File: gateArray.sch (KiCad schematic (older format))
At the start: 56 parts, among them IC101 AMS40489, IC108 MC74HC4051N, IC109 LA6393D, X181 40MhZ

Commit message: more accurate on pins definition, power, centronic 36, jack, and some wiring
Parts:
- removed C128: 39P, symbol Device:C_Small
- removed C129: 47P, symbol Device:C_Small
- removed L102: L, symbol Device:L
- removed R145: 4,7M, symbol Device:R_Small_US
- removed X181: 40MhZ, Oscillator:Oscillator_DIP-8, symbol Device:Crystal
- added X181: 40 MHz, Oscillator:Oscillator_DIP-14, symbol Oscillator:ACO-xxxMHz
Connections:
- wire segments 409 -> 387
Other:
- note removed: "40MhZ\nOSC"
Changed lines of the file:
@@
 Wire Wire Line
 	6950 5550 6850 5550
-Wire Wire Line
-	7250 5400 7250 6500
 $Comp
 L power:+5V #PWR0113
@@
 Connection ~ 2850 4050
 Wire Wire Line
-	2850 4050 2500 4050
-Wire Wire Line
 	3200 3200 3200 3100
 Wire Wire Line
@@
 Wire Wire Line
 	2050 3950 2050 4050
-Wire Wire Line
-	2350 4050 2050 4050
 Connection ~ 2050 4050
 Wire Wire Line
@@
 	1    0    0    -1
 $EndComp
-$Comp
-L Device:C_Small C128
-U 1 1 6120AEE9
-P 6450 7050
-F 0 "C128" H 6542 7096 50  0000 L CNN
-F 1 "39P" H 6542 7005 50  0000 L CNN
-F 2 "" H 6450 7050 50  0001 C CNN
-F 3 "~" H 6450 7050 50  0001 C CNN
-	1    6450 7050
-	1    0    0    -1
-$EndComp
 Wire Wire Line
 	5100 7400 5150 7400
@@
 Wire Wire Line
 	4550 7400 4600 7400
-Wire Wire Line
-	6450 7150 6450 7250
 $Comp
 L power:GND #PWR0106
 U 1 1 61400741
-P 6800 7350
-F 0 "#PWR0106" H 6800 7100 50  0001 C CNN
-F 1 "GND" H 6805 7177 50  0000 C CNN
-F 2 "" H 6800 7350 50  0001 C CNN
-F 3 "" H 6800 7350 50  0001 C CNN
-	1    6800 7350
+P 6850 6600
+F 0 "#PWR0106" H 6850 6350 50  0001 C CNN
+F 1 "GND" H 6855 6427 50  0000 C CNN
+F 2 "" H 6850 6600 50  0001 C CNN
+F 3 "" H 6850 6600 50  0001 C CNN
+	1    6850 6600
 	1    0    0    -1
 $EndComp
@@
 	6350 5400 6350 6800
 Wire Wire Line
-	7150 5400 7150 6350
+	7150 5400 7150 6300
 Wire Wire Line
 	6050 6950 6050 6800
@@
 Wire Wire Line
 	4550 6300 5850 6300
-$Comp
-L Device:C_Small C129
-U 1 1 61627E90
-P 7150 7050
-F 0 "C129" H 7242 7096 50  0000 L CNN
-F 1 "47P" H 7242 7005 50  0000 L CNN
-F 2 "" H 7150 7050 50  0001 C CNN
-F 3 "~" H 7150 7050 50  0001 C CNN
-	1    7150 7050
-	1    0    0    -1
-$EndComp
 Wire Wire Line
 	6550 5400 6550 6200
@@
 	1400 5150 5150 5150
 Wire Wire Line
-	6650 6000 6850 6000
-Wire Wire Line
-	6850 6000 6850 5900
-Wire Wire Line
-	6650 5550 6650 6000
+	6850 6000 6850 5950
 $Comp
 L 6128:LA6393D IC109
@@
 Wire Wire Line
 	10300 4150 10300 6600
-$Comp
-L Device:Crystal Y?
-U 1 1 6056C8D5
-P 6800 6850
-AR Path="/6056C8D5" Ref="Y?"  Part="1"
-AR Path="/604FCFA4/6056C8D5" Ref="X181"  Part="1"
-F 0 "X181" H 6800 7118 50  0000 C CNN
-F 1 "40MhZ" H 6800 7027 50  0000 C CNN
-F 2 "Oscillator:Oscillator_DIP-8" H 6800 6850 50  0001 C CNN
-F 3 "~" H 6800 6850 50  0001 C CNN
-	1    6800 6850
-	1    0    0    -1
-$EndComp
-$Comp
-L Device:L L102
-U 1 1 605A0F1D
-P 7450 7050
-F 0 "L102" H 7503 7096 50  0000 L CNN
-F 1 "L" H 7503 7005 50  0000 L CNN
-F 2 "" H 7450 7050 50  0001 C CNN
-F 3 "~" H 7450 7050 50  0001 C CNN
-	1    7450 7050
-	1    0    0    -1
-$EndComp
-$Comp
-L Device:R_Small_US R145
-U 1 1 605A2790
-P 6800 6500
-F 0 "R145" V 7005 6500 50  0000 C CNN
-F 1 "4,7M" V 6914 6500 50  0000 C CNN
-F 2 "" H 6800 6500 50  0001 C CNN
-F 3 "~" H 6800 6500 50  0001 C CNN
-	1    6800 6500
-	0    -1   -1   0
-$EndComp
-Wire Wire Line
-	7150 6350 6450 6350
-Wire Wire Line
-	6450 6350 6450 6850
-Wire Wire Line
-	6450 6850 6550 6850
-Connection ~ 6450 6850
-Wire Wire Line
-	6450 6850 6450 6950
-Wire Wire Line
-	6950 6850 7050 6850
-Wire Wire Line
-	6550 6850 6550 6500
-Wire Wire Line
-	6550 6500 6700 6500
-Connection ~ 6550 6850
-Wire Wire Line
-	6550 6850 6650 6850
-Wire Wire Line
-	6900 6500 7050 6500
-Wire Wire Line
-	7050 6500 7050 6850
-Connection ~ 7050 6850
-Wire Wire Line
-	7050 6850 7150 6850
-Wire Wire Line
-	7150 6850 7150 6950
-Wire Wire Line
-	7150 7150 7150 7250
-Wire Wire Line
-	7150 7250 6800 7250
-Wire Wire Line
-	6800 7250 6450 7250
-Connection ~ 6800 7250
-Wire Wire Line
-	6800 7250 6800 7350
-Wire Wire Line
-	7150 6850 7450 6850
-Wire Wire Line
-	7450 6850 7450 6900
-Connection ~ 7150 6850
-Wire Wire Line
-	7150 7250 7450 7250
 Wire Wire Line
 	7450 7250 7450 7200
-Connection ~ 7150 7250
-Wire Wire Line
-	7150 6850 7150 6500
-Wire Wire Line
-	7150 6500 7250 6500
 $Comp
 L Device:C_Small C101
@@
 Text Notes 2000 1250 0    39   ~ 0
 CAPS DISTRIBUTED\nEVENLY AROUND IC101
-Text Notes 6700 6200 0    39   ~ 0
-40MhZ\nOSC
 $Comp
 L Device:CP1 C126
@@
 Wire Wire Line
 	9850 2650 10100 2650
+$Comp
+L Oscillator:ACO-xxxMHz X181
+U 1 1 6062CA28
+P 6850 6300
+F 0 "X181" H 6507 6346 50  0000 R CNN
+F 1 "40 MHz" H 6507 6255 50  0000 R CNN
+F 2 "Oscillator:Oscillator_DIP-14" H 6507 6209 50  0001 R CNN
+F 3 "http://www.conwin.com/datasheets/cx/cx030.pdf" H 6750 6300 50  0001 C CNN
+	1    6850 6300
+	1    0    0    -1
+$EndComp
+Wire Wire Line
+	6650 5550 6650 5950
+Wire Wire Line
+	6850 5950 6650 5950
+Connection ~ 6850 5950
+Wire Wire Line
+	6850 5950 6850 5900
+Wire Wire Line
+	2500 4050 2850 4050
+Wire Wire Line
+	2050 4050 2350 4050
 Wire Bus Line
 	9900 6700 10350 6700

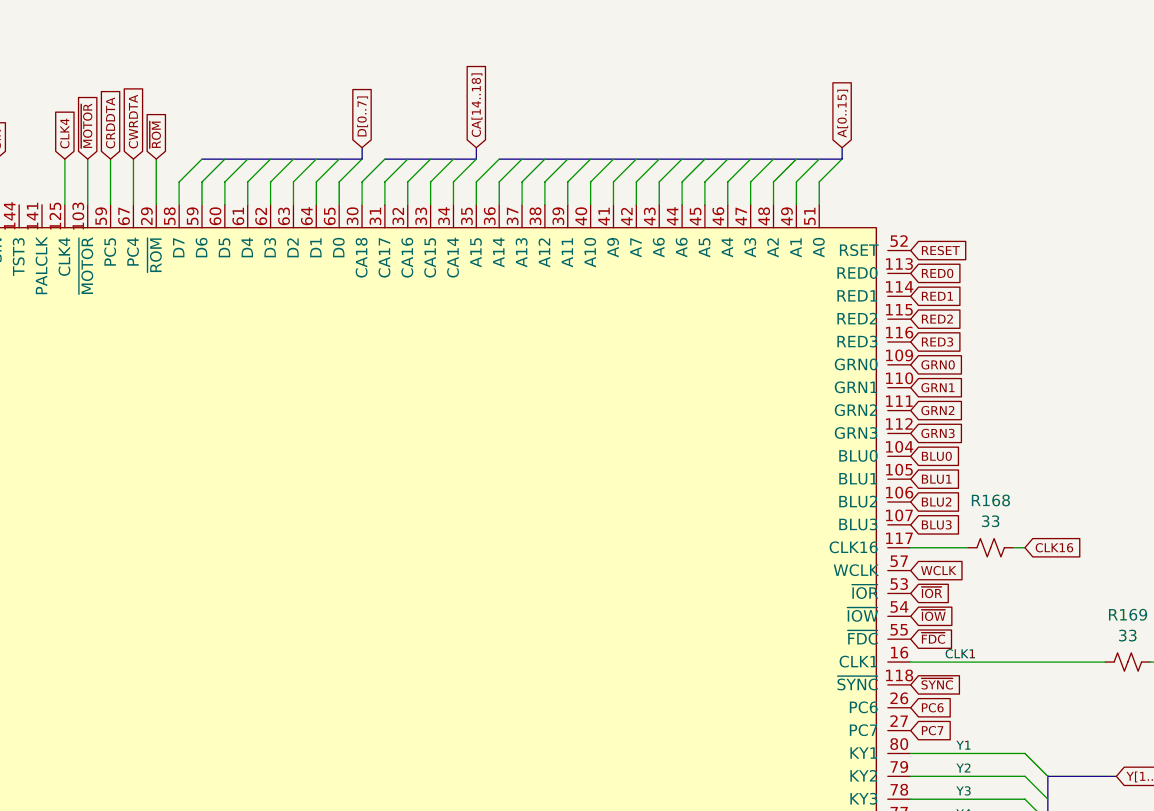
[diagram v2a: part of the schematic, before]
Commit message: 29-03-2021 : first usage of hierarchical labels. focus on CPU/ Cartridge Connector
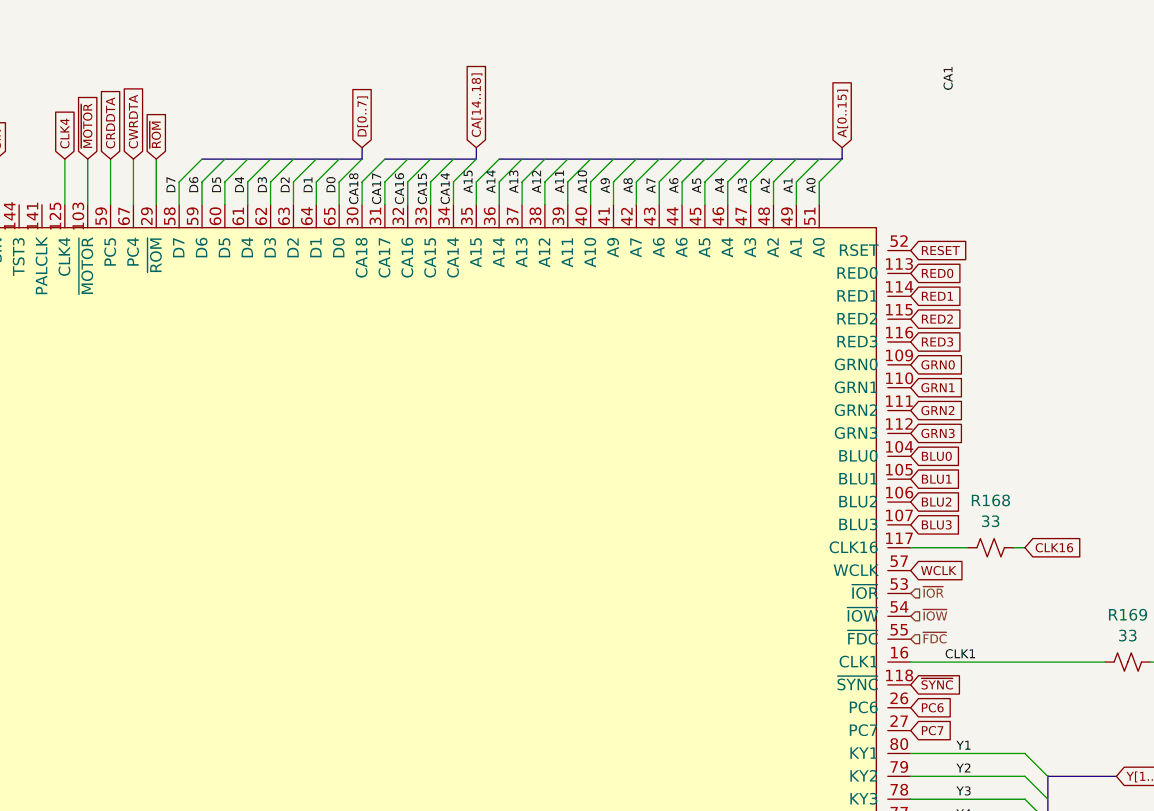
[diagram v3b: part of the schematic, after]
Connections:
- net labels added: A0, A1, A10, A11, A12, A13, A14, A15, A2, A3, A4, A5, A6, A7, A8, A9, CA1, CA14, CA15, CA16, CA17, CA18, D0, D1, D2, D3, D4, D5, D6, D7
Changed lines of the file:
@@
 Text GLabel 9850 2750 2    39   Input ~ 0
 WCLK
-Text GLabel 9850 2850 2    39   Input ~ 0
-~IOR
-Text GLabel 9850 2950 2    39   Input ~ 0
-~IOW
-Text GLabel 9850 3050 2    39   Input ~ 0
-~FDC
 Text GLabel 10950 3150 2    39   Input ~ 0
 CLK1
@@
 Text Label 10050 4450 0    39   ~ 0
 Y10
+Text Label 7350 1100 1    39   ~ 0
+D0
+Text Label 7250 1100 1    39   ~ 0
+D1
+Text Label 7150 1100 1    39   ~ 0
+D2
+Text Label 7050 1100 1    39   ~ 0
+D3
+Text Label 6950 1100 1    39   ~ 0
+D4
+Text Label 6850 1100 1    39   ~ 0
+D5
+Text Label 6750 1100 1    39   ~ 0
+D6
+Text Label 6650 1100 1    39   ~ 0
+D7
+Text Label 9450 1100 1    39   ~ 0
+A0
+Text Label 9350 1100 1    39   ~ 0
+A1
+Text Label 9250 1100 1    39   ~ 0
+A2
+Text Label 9150 1100 1    39   ~ 0
+A3
+Text Label 9050 1100 1    39   ~ 0
+A4
+Text Label 8950 1100 1    39   ~ 0
+A5
+Text Label 8850 1100 1    39   ~ 0
+A6
+Text Label 8750 1100 1    39   ~ 0
+A7
+Text Label 8650 1100 1    39   ~ 0
+A8
+Text Label 8550 1100 1    39   ~ 0
+A9
+Text Label 8450 1100 1    39   ~ 0
+A10
+Text Label 8350 1100 1    39   ~ 0
+A11
+Text Label 8250 1100 1    39   ~ 0
+A12
+Text Label 8150 1100 1    39   ~ 0
+A13
+Text Label 8050 1100 1    39   ~ 0
+A14
+Text Label 7950 1100 1    39   ~ 0
+A15
+Text Label 10050 650  1    39   ~ 0
+CA1
+Text Label 7850 1150 1    39   ~ 0
+CA14
+Text Label 7750 1150 1    39   ~ 0
+CA15
+Text Label 7650 1150 1    39   ~ 0
+CA16
+Text Label 7550 1150 1    39   ~ 0
+CA17
+Text Label 7450 1150 1    39   ~ 0
+CA18
+Text HLabel 9850 2850 2    39   Input ~ 0
+~IOR
+Text HLabel 9850 2950 2    39   Input ~ 0
+~IOW
+Text HLabel 9850 3050 2    39   Input ~ 0
+~FDC
 Wire Bus Line
 	9900 6700 10350 6700

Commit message: finished work on Z80
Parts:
- X181: footprint Oscillator:Oscillator_DIP-14 -> cpc6128+:Oscillator_X181_DIP-14
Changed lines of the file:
@@
 F 0 "X181" H 6507 6346 50  0000 R CNN
 F 1 "40 MHz" H 6507 6255 50  0000 R CNN
-F 2 "Oscillator:Oscillator_DIP-14" H 6507 6209 50  0001 R CNN
+F 2 "cpc6128+:Oscillator_X181_DIP-14" H 6507 6209 50  0001 R CNN
 F 3 "http://www.conwin.com/datasheets/cx/cx030.pdf" H 6750 6300 50  0001 C CNN
 	1    6850 6300

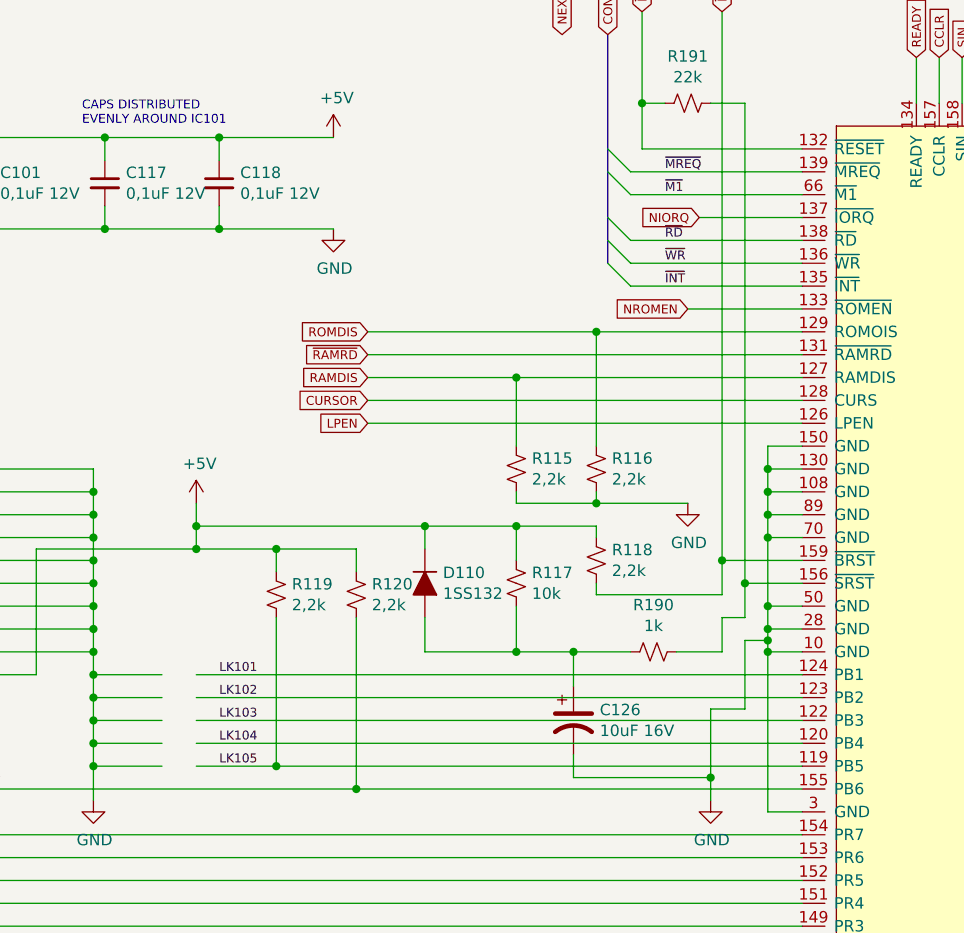
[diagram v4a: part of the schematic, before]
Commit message: More work on centronics port.
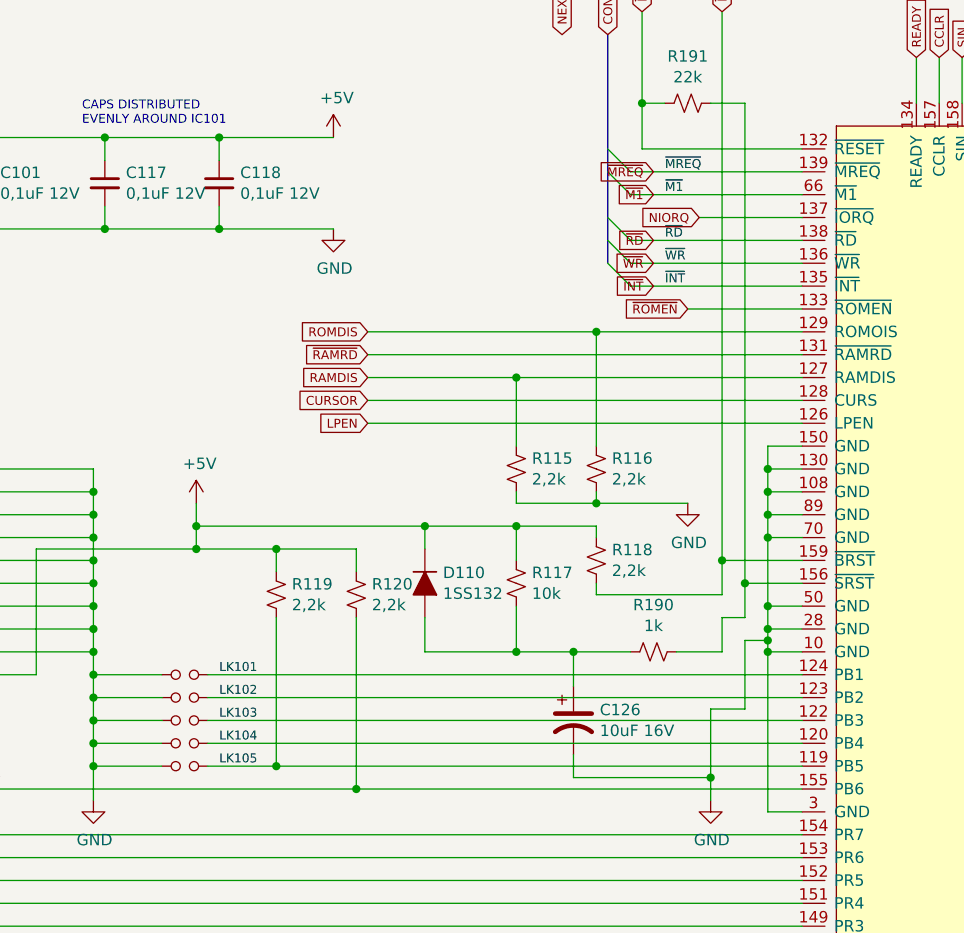
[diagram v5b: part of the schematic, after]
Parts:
- added LK101, LK102, LK103, LK104, LK105: Jumper_NO_Small, symbol Device:Jumper_NO_Small
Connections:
- net labels added: ~ROMEN
- net labels removed: NROMEN
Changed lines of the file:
@@
 NEXP
 Text GLabel 4650 2050 0    39   Input ~ 0
-NROMEN
+~ROMEN
 Wire Wire Line
 	5150 2650 5000 2650
@@
 +5V
 Wire Wire Line
-	5150 3650 2500 3650
-Wire Wire Line
-	5150 3750 2500 3750
-Wire Wire Line
-	5150 3850 2500 3850
-Wire Wire Line
-	5150 3950 2500 3950
+	5150 3650 2550 3650
+Wire Wire Line
+	5150 3750 2550 3750
+Wire Wire Line
+	5150 3850 2550 3850
 Wire Wire Line
 	5150 4050 2850 4050
@@
 Wire Wire Line
 	6850 5950 6850 5900
-Wire Wire Line
-	2500 4050 2850 4050
 Wire Wire Line
 	2050 4050 2350 4050
@@
 Text HLabel 9850 3050 2    39   Input ~ 0
 ~FDC
+Text GLabel 4500 1550 0    39   Input ~ 0
+~M1
+Text GLabel 4500 1750 0    39   Input ~ 0
+~RD
+Text GLabel 4500 1850 0    39   Input ~ 0
+~WR
+Text GLabel 4500 1950 0    39   Input ~ 0
+~INT
+Text GLabel 4500 1450 0    39   Input ~ 0
+~MREQ
+$Comp
+L Device:Jumper_NO_Small LK105
+U 1 1 60769E4F
+P 2450 4050
+F 0 "LK105" H 2450 4143 50  0001 C CNN
+F 1 "Jumper_NO_Small" H 2450 4144 50  0001 C CNN
+F 2 "" H 2450 4050 50  0001 C CNN
+F 3 "~" H 2450 4050 50  0001 C CNN
+	1    2450 4050
+	1    0    0    -1
+$EndComp
+Wire Wire Line
+	2550 4050 2850 4050
+$Comp
+L Device:Jumper_NO_Small LK104
+U 1 1 607CB8B3
+P 2450 3950
+F 0 "LK104" H 2450 4135 50  0001 C CNN
+F 1 "Jumper_NO_Small" H 2450 4044 50  0001 C CNN
+F 2 "" H 2450 3950 50  0001 C CNN
+F 3 "~" H 2450 3950 50  0001 C CNN
+	1    2450 3950
+	1    0    0    -1
+$EndComp
+Wire Wire Line
+	5150 3950 2550 3950
+$Comp
+L Device:Jumper_NO_Small LK103
+U 1 1 607FC508
+P 2450 3850
+F 0 "LK103" H 2450 3943 50  0001 C CNN
+F 1 "Jumper_NO_Small" H 2450 3944 50  0001 C CNN
+F 2 "" H 2450 3850 50  0001 C CNN
+F 3 "~" H 2450 3850 50  0001 C CNN
+	1    2450 3850
+	1    0    0    -1
+$EndComp
+$Comp
+L Device:Jumper_NO_Small LK102
+U 1 1 607FD1A8
+P 2450 3750
+F 0 "LK102" H 2450 3935 50  0001 C CNN
+F 1 "Jumper_NO_Small" H 2450 3843 50  0001 C CNN
+F 2 "" H 2450 3750 50  0001 C CNN
+F 3 "~" H 2450 3750 50  0001 C CNN
+	1    2450 3750
+	1    0    0    -1
+$EndComp
+$Comp
+L Device:Jumper_NO_Small LK101
+U 1 1 6085EDA7
+P 2450 3650
+F 0 "LK101" H 2450 3835 50  0001 C CNN
+F 1 "Jumper_NO_Small" H 2450 3744 50  0001 C CNN
+F 2 "" H 2450 3650 50  0001 C CNN
+F 3 "~" H 2450 3650 50  0001 C CNN
+	1    2450 3650
+	1    0    0    -1
+$EndComp
 Wire Bus Line
 	9900 6700 10350 6700
